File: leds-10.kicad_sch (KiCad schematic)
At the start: 20 parts

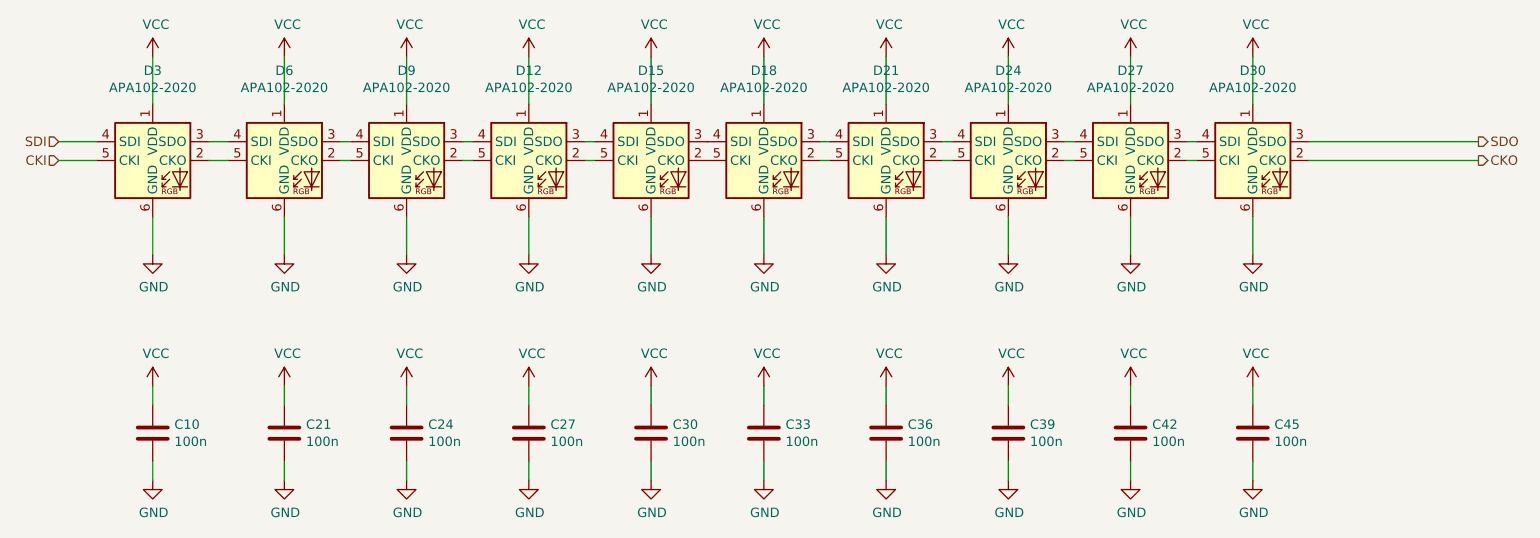
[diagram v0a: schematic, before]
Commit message: Convert to KiCad7, add iBOM
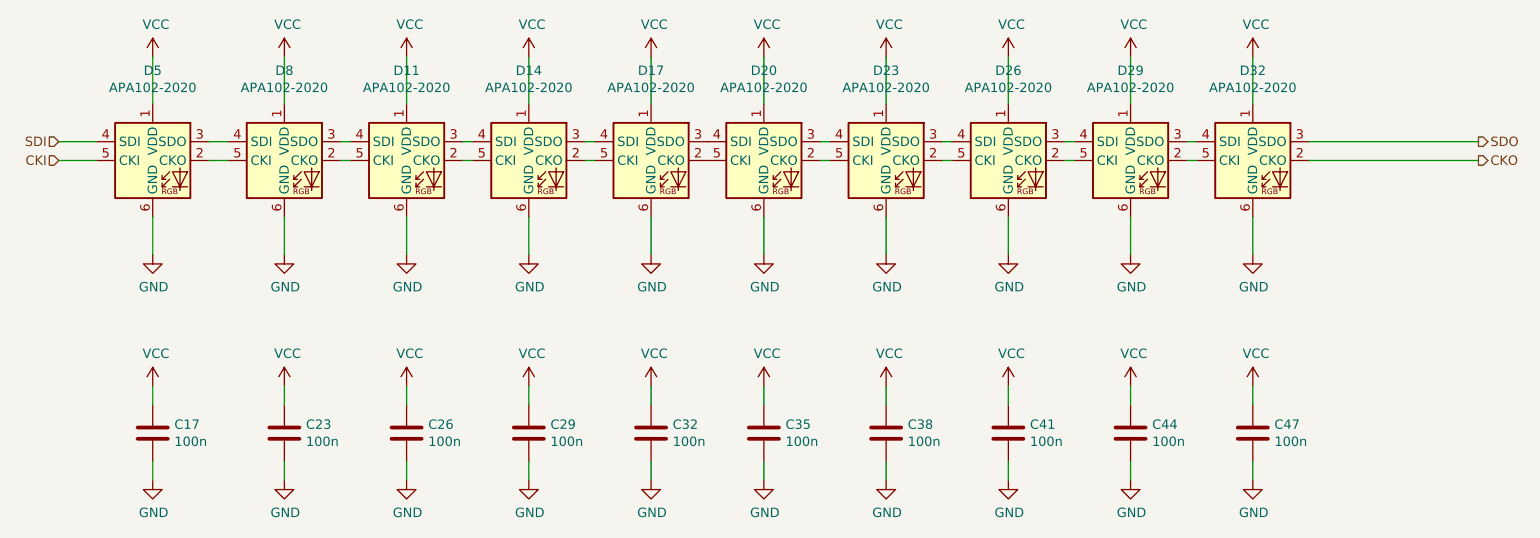
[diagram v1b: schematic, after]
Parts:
- renumbered C10 to C17, C21 to C23, C24 to C26, C27 to C29, C30 to C32, C33 to C35, C36 to C38, C39 to C41, C42 to C44, C45 to C47, D9 to D11, D12 to D14, D15 to D17, D18 to D20, D21 to D23, D24 to D26, D27 to D29, D30 to D32, D3 to D5, D6 to D8
